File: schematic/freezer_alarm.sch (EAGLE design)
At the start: 5 parts, among them IC1 DS18B20+, IC2 DS18B20+

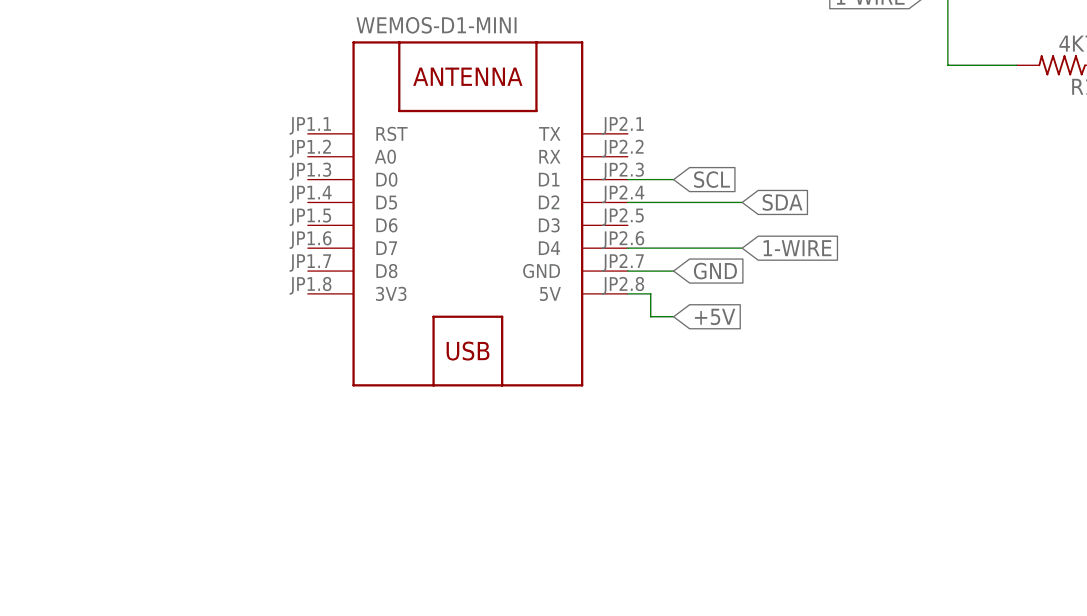
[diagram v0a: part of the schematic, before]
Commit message: Moved arrduino files to src
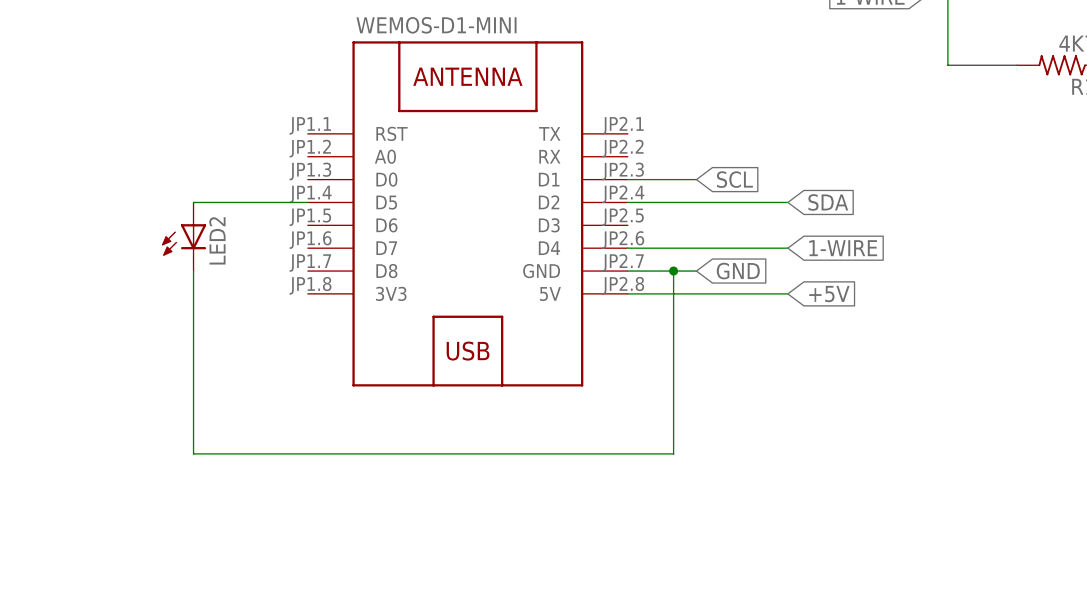
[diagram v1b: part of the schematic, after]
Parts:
- added LED2: (no value), adafruit:LED5MM
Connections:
- new net N$1: LED2.A, W1.D5
- net GND: now also LED2.C
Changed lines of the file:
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@@
 <setting verticaltext="up"/>
 </settings>
-<grid distance="0.1" unitdist="inch" unit="inch" style="lines" multiple="1" display="no" altdistance="0.01" altunitdist="inch" altunit="inch"/>
+<grid distance="0.1" unitdist="inch" unit="inch" style="lines" multiple="1" display="yes" altdistance="0.01" altunitdist="inch" altunit="inch"/>
 <layers>
 <layer number="1" name="Top" color="4" fill="1" visible="no" active="no"/>
@@
 <part name="IC2" library="SamacSys_Parts" deviceset="DS18B20+" device=""/>
 <part name="R1" library="adafruit" library_urn="urn:adsk.eagle:library:420" deviceset="R-US_" device="0207/10" package3d_urn="urn:adsk.eagle:package:6240597/1" value="4K7"/>
+<part name="LED2" library="adafruit" library_urn="urn:adsk.eagle:library:420" deviceset="LED" device="5MM" package3d_urn="urn:adsk.eagle:package:6240538/1"/>
 </parts>
 <sheets>
@@
 <attribute name="VALUE" x="191.77" y="148.082" size="1.778" layer="96" rot="R180"/>
 </instance>
+<instance part="LED2" gate="G$1" x="91.44" y="127" smashed="yes">
+<attribute name="NAME" x="94.996" y="122.428" size="1.778" layer="95" rot="R90"/>
+<attribute name="VALUE" x="97.155" y="122.428" size="1.778" layer="96" rot="R90"/>
+</instance>
 </instances>
 <busses>
@@
 <segment>
 <pinref part="W1" gate="G$1" pin="5V"/>
-<wire x1="139.7" y1="119.38" x2="142.24" y2="119.38" width="0.1524" layer="91"/>
-<wire x1="142.24" y1="119.38" x2="142.24" y2="116.84" width="0.1524" layer="91"/>
-<wire x1="142.24" y1="116.84" x2="144.78" y2="116.84" width="0.1524" layer="91"/>
-<label x="144.78" y="116.84" size="1.778" layer="95" xref="yes"/>
+<wire x1="139.7" y1="119.38" x2="157.48" y2="119.38" width="0.1524" layer="91"/>
+<label x="157.48" y="119.38" size="1.778" layer="95" xref="yes"/>
 </segment>
 <segment>
@@
 </net>
 <net name="GND" class="0">
-<segment>
-<pinref part="W1" gate="G$1" pin="GND"/>
-<wire x1="139.7" y1="121.92" x2="144.78" y2="121.92" width="0.1524" layer="91"/>
-<label x="144.78" y="121.92" size="1.778" layer="95" xref="yes"/>
-</segment>
 <segment>
 <pinref part="DISP" gate="G$1" pin="GND"/>
@@
 <label x="172.72" y="172.72" size="1.778" layer="95" rot="R180" xref="yes"/>
 </segment>
+<segment>
+<pinref part="W1" gate="G$1" pin="GND"/>
+<wire x1="139.7" y1="121.92" x2="144.78" y2="121.92" width="0.1524" layer="91"/>
+<pinref part="LED2" gate="G$1" pin="C"/>
+<wire x1="144.78" y1="121.92" x2="147.32" y2="121.92" width="0.1524" layer="91"/>
+<wire x1="91.44" y1="121.92" x2="91.44" y2="101.6" width="0.1524" layer="91"/>
+<wire x1="91.44" y1="101.6" x2="144.78" y2="101.6" width="0.1524" layer="91"/>
+<wire x1="144.78" y1="101.6" x2="144.78" y2="121.92" width="0.1524" layer="91"/>
+<junction x="144.78" y="121.92"/>
+<label x="147.32" y="121.92" size="1.778" layer="95" xref="yes"/>
+</segment>
 </net>
 <net name="SDA" class="0">
@@
 <segment>
 <pinref part="W1" gate="G$1" pin="D2"/>
-<wire x1="139.7" y1="129.54" x2="152.4" y2="129.54" width="0.1524" layer="91"/>
-<label x="152.4" y="129.54" size="1.778" layer="95" xref="yes"/>
+<wire x1="139.7" y1="129.54" x2="157.48" y2="129.54" width="0.1524" layer="91"/>
+<label x="157.48" y="129.54" size="1.778" layer="95" xref="yes"/>
 </segment>
 </net>
@@
 <segment>
 <pinref part="W1" gate="G$1" pin="D1"/>
-<wire x1="139.7" y1="132.08" x2="144.78" y2="132.08" width="0.1524" layer="91"/>
-<label x="144.78" y="132.08" size="1.778" layer="95" xref="yes"/>
+<wire x1="139.7" y1="132.08" x2="147.32" y2="132.08" width="0.1524" layer="91"/>
+<label x="147.32" y="132.08" size="1.778" layer="95" xref="yes"/>
 </segment>
 </net>
@@
 <segment>
 <pinref part="W1" gate="G$1" pin="D4"/>
-<wire x1="139.7" y1="124.46" x2="152.4" y2="124.46" width="0.1524" layer="91"/>
-<label x="152.4" y="124.46" size="1.778" layer="95" xref="yes"/>
+<wire x1="139.7" y1="124.46" x2="157.48" y2="124.46" width="0.1524" layer="91"/>
+<label x="157.48" y="124.46" size="1.778" layer="95" xref="yes"/>
 </segment>
 <segment>
@@
 </segment>
 </net>
+<net name="N$1" class="0">
+<segment>
+<pinref part="W1" gate="G$1" pin="D5"/>
+<pinref part="LED2" gate="G$1" pin="A"/>
+<wire x1="104.14" y1="129.54" x2="91.44" y2="129.54" width="0.1524" layer="91"/>
+</segment>
+</net>

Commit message: Added R2
Added R2
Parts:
- added R2: 1K, adafruit:R-US_0207/10
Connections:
- new net N$2: LED2.C, R2.1
- net GND: now also R2.2; no longer LED2.C
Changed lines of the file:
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@@
 <?xml version="1.0" encoding="utf-8"?>
 <!DOCTYPE eagle SYSTEM "eagle.dtd">
-<eagle version="9.3.2">
+<eagle version="9.6.2">
 <drawing>
 <settings>
@@
 <part name="R1" library="adafruit" library_urn="urn:adsk.eagle:library:420" deviceset="R-US_" device="0207/10" package3d_urn="urn:adsk.eagle:package:6240597/1" value="4K7"/>
 <part name="LED2" library="adafruit" library_urn="urn:adsk.eagle:library:420" deviceset="LED" device="5MM" package3d_urn="urn:adsk.eagle:package:6240538/1"/>
+<part name="R2" library="adafruit" library_urn="urn:adsk.eagle:library:420" deviceset="R-US_" device="0207/10" package3d_urn="urn:adsk.eagle:package:6240597/1" value="1K"/>
 </parts>
 <sheets>
@@
 <attribute name="VALUE" x="97.155" y="122.428" size="1.778" layer="96" rot="R90"/>
 </instance>
+<instance part="R2" gate="G$1" x="91.44" y="114.3" smashed="yes" rot="R270">
+<attribute name="NAME" x="92.9386" y="118.11" size="1.778" layer="95" rot="R270"/>
+<attribute name="VALUE" x="88.138" y="118.11" size="1.778" layer="96" rot="R270"/>
+</instance>
 </instances>
 <busses>
@@
 <pinref part="W1" gate="G$1" pin="GND"/>
 <wire x1="139.7" y1="121.92" x2="144.78" y2="121.92" width="0.1524" layer="91"/>
-<pinref part="LED2" gate="G$1" pin="C"/>
 <wire x1="144.78" y1="121.92" x2="147.32" y2="121.92" width="0.1524" layer="91"/>
-<wire x1="91.44" y1="121.92" x2="91.44" y2="101.6" width="0.1524" layer="91"/>
 <wire x1="91.44" y1="101.6" x2="144.78" y2="101.6" width="0.1524" layer="91"/>
 <wire x1="144.78" y1="101.6" x2="144.78" y2="121.92" width="0.1524" layer="91"/>
 <junction x="144.78" y="121.92"/>
 <label x="147.32" y="121.92" size="1.778" layer="95" xref="yes"/>
+<pinref part="R2" gate="G$1" pin="2"/>
+<wire x1="91.44" y1="109.22" x2="91.44" y2="101.6" width="0.1524" layer="91"/>
 </segment>
 </net>
@@
 </segment>
 </net>
+<net name="N$2" class="0">
+<segment>
+<pinref part="LED2" gate="G$1" pin="C"/>
+<pinref part="R2" gate="G$1" pin="1"/>
+<wire x1="91.44" y1="121.92" x2="91.44" y2="119.38" width="0.1524" layer="91"/>
+</segment>
+</net>
